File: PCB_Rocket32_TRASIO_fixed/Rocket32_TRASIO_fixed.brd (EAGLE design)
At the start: 167.6 x 111.8 mm, 65 parts, among them IC1 TXB0108PWR, IC2 TXB0108PWR, IC3 AMS1117-1.8, IC5 AMS1117-1.8, J1 2985-6004, J2 2985-6004, J4 2985-6004, J5 2985-6004, Q5 2N7002K-7, Q6 2N7002K-7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

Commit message: Update position of Flash
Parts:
- moved JTAG_20_PIN 25.2 mm to (-66.0, 49.5), turned to 0 degrees
- moved FLASH 15.2 mm to (-85.1, 25.4)
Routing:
- net TCK: track 16.1 -> 43.4 mm
- net TMS: track 15.3 -> 42.4 mm
- net TDO: track 20.5 -> 46.9 mm
- net GND: track 2121.9 -> 2148.2 mm
- net VDD_3V3: track 232.9 -> 249.0 mm, vias 0 -> 1
- net TDI: track 13.5 -> 29.3 mm
- net FLASH_CS: track 32.5 -> 25.6 mm
- net FLASH_MOSI: track 18.7 -> 13.5 mm
- net FLASH_MISO: track 17.1 -> 14.0 mm
- net MEMSER_IN_BITS[7]: track 162.2 -> 159.7 mm
- net MEMSER_IN_BITS[6]: track 160.5 -> 158.1 mm
- net FLASH_SCK: track 16.1 -> 14.9 mm
- net MEMSER_IN_BITS[5]: track 159.8 -> 158.9 mm

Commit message: Fix SD card position
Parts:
- moved SD_CARD 9.51 mm to (-84.6, -3.20)
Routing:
- net GND: track 2148.2 -> 2161.4 mm
- net MOSI: track 25.2 -> 15.6 mm
- net MISO: track 23.3 -> 14.8 mm
- net SCLK: track 21.5 -> 14.1 mm
- net CS: track 36.2 -> 28.8 mm

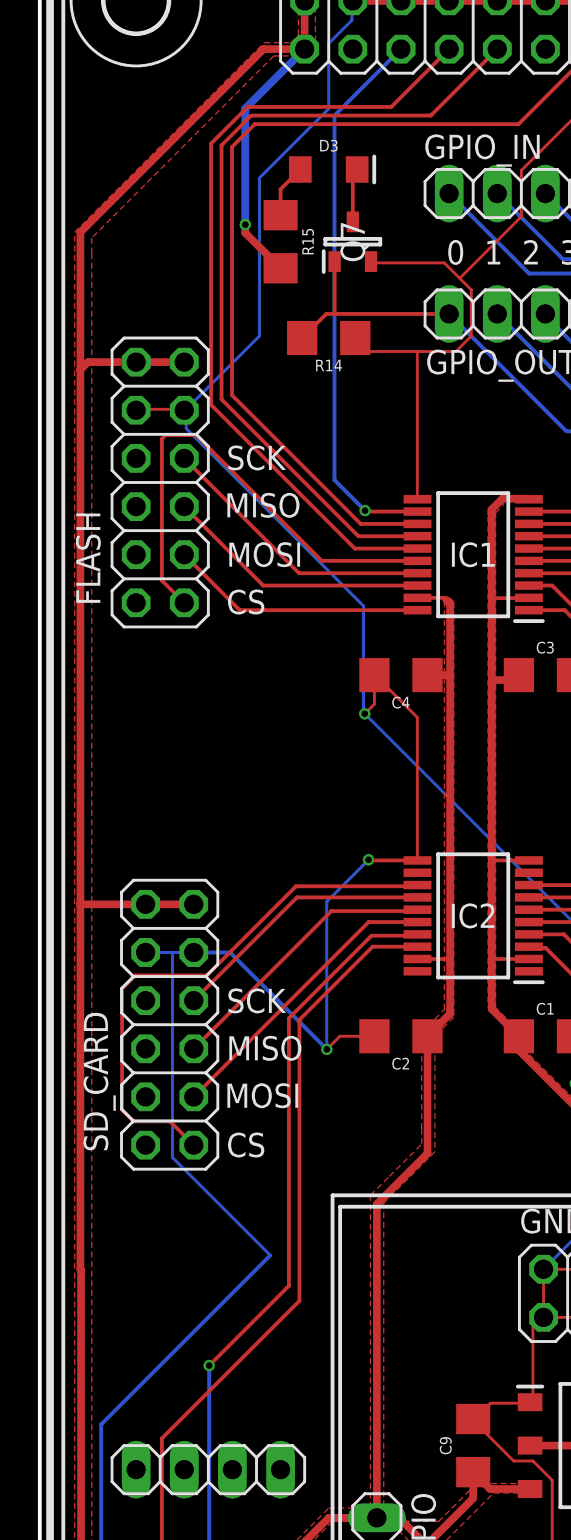
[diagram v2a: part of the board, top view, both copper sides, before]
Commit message: Update position of SD card again
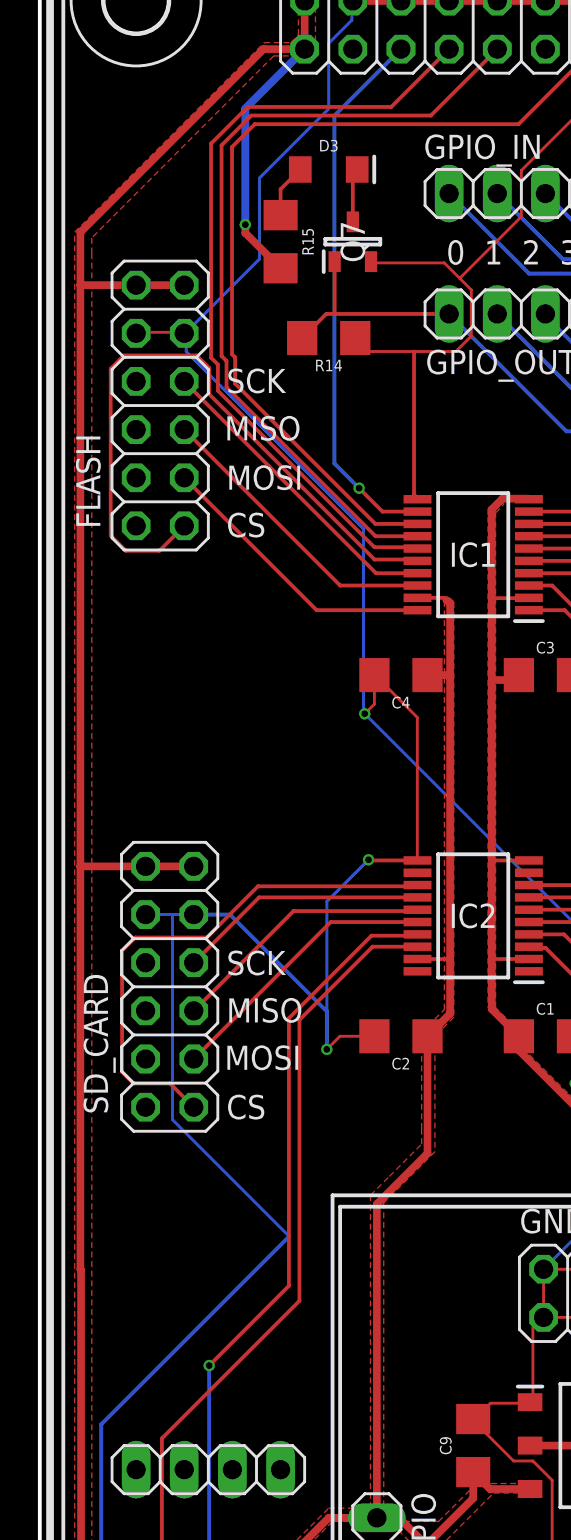
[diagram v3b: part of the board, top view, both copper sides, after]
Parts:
- moved FLASH 4.06 mm to (-85.1, 29.5)
- moved SD_CARD 2.00 mm to (-84.6, -1.20)
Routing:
- net FLASH_CS: track 25.5 -> 35.3 mm
- net GND: track 2161.4 -> 2166.3 mm
- net FLASH_MISO: track 14.0 -> 15.7 mm
- net FLASH_MOSI: track 13.5 -> 15.2 mm
- net FLASH_SCK: track 14.8 -> 16.5 mm
- net SCLK: track 14.1 -> 13.2 mm
- net MOSI: track 15.6 -> 14.8 mm
- net MISO: track 14.8 -> 14.0 mm
- net CS: track 28.8 -> 28.0 mm
- net TMS: track 42.4 -> 41.8 mm
- net TCK: track 43.4 -> 42.8 mm
- net TDI: track 29.3 -> 28.7 mm

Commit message: This should work man
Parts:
- moved FLASH 8.86 mm to (-86.3, 38.2)
- moved USB-UART_1 1.50 mm to (-82.5, -35.8)
- moved USB-UART_2 1.50 mm to (-82.5, -28.2)
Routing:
- net GND: track 2166.3 -> 2154.4 mm, vias 504 -> 505
- net FLASH_SCK: track 16.5 -> 25.8 mm
- net FLASH_CS: track 35.3 -> 44.4 mm
- net FLASH_MISO: track 15.7 -> 23.9 mm
- net FLASH_MOSI: track 15.2 -> 22.4 mm
- net TCK: track 42.8 -> 40.8 mm
- net TDO: track 46.4 -> 44.5 mm
- net TMS: track 41.8 -> 40.1 mm
- net TX: track 43.3 -> 44.8 mm
- net RX: track 42.7 -> 44.2 mm
- net VDD_3V3: track 249.3 -> 248.5 mm
